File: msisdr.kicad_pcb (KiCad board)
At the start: 2 copper layers, 46.3 x 90.7 mm, 70 parts, among them J1 VCC_GPIO, J10 SMA_VHF1, J11 USB_OTG, J2 GPIO0, J3 GPIO1, J4 GPIO2, J5 GPIO3, J6 SMA_0_30MHZ, J7 SMA_30_60MHZ, J8 SMA_VHF2, J9 SMA_UHF, U1 msi2500, U2 msi001, U3 LP5900SDX-2.8, U4 AP7313-30SAG, Y1 24MHz

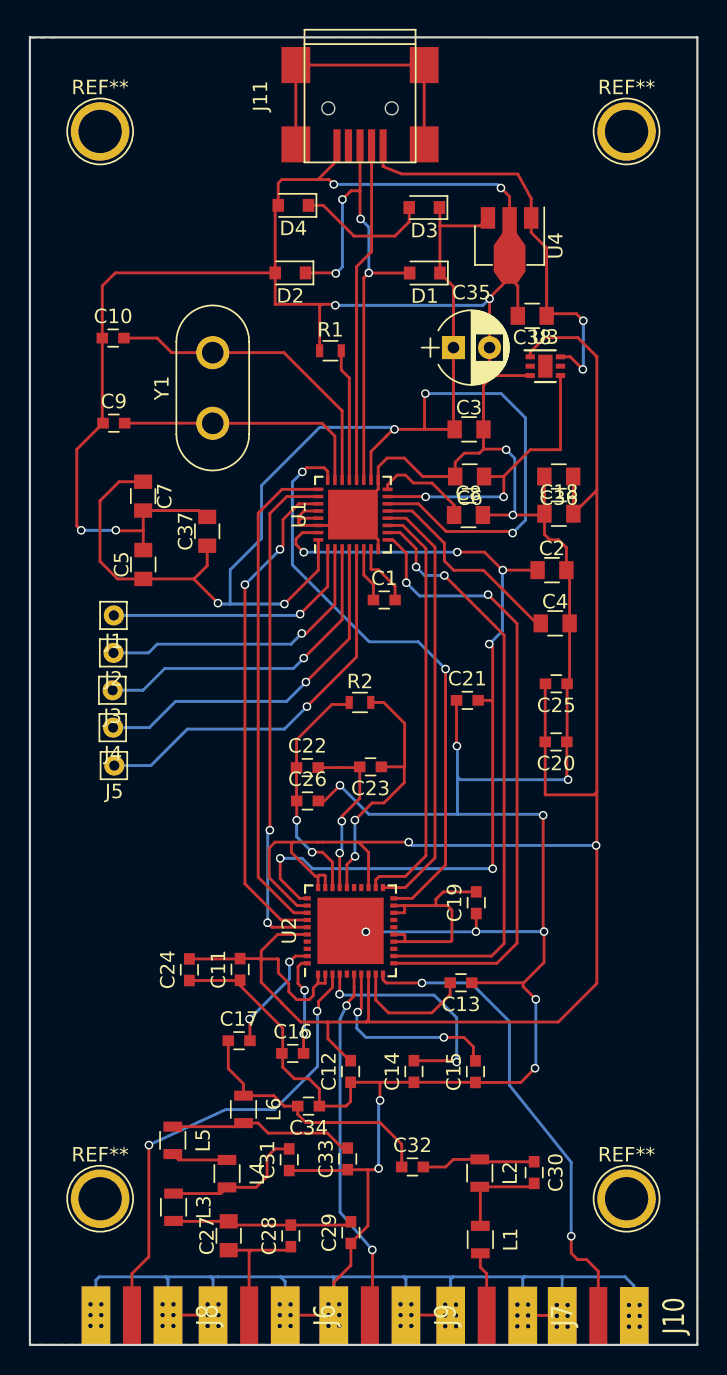
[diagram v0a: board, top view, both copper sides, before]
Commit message: use external oscillator repace xtal and add a led
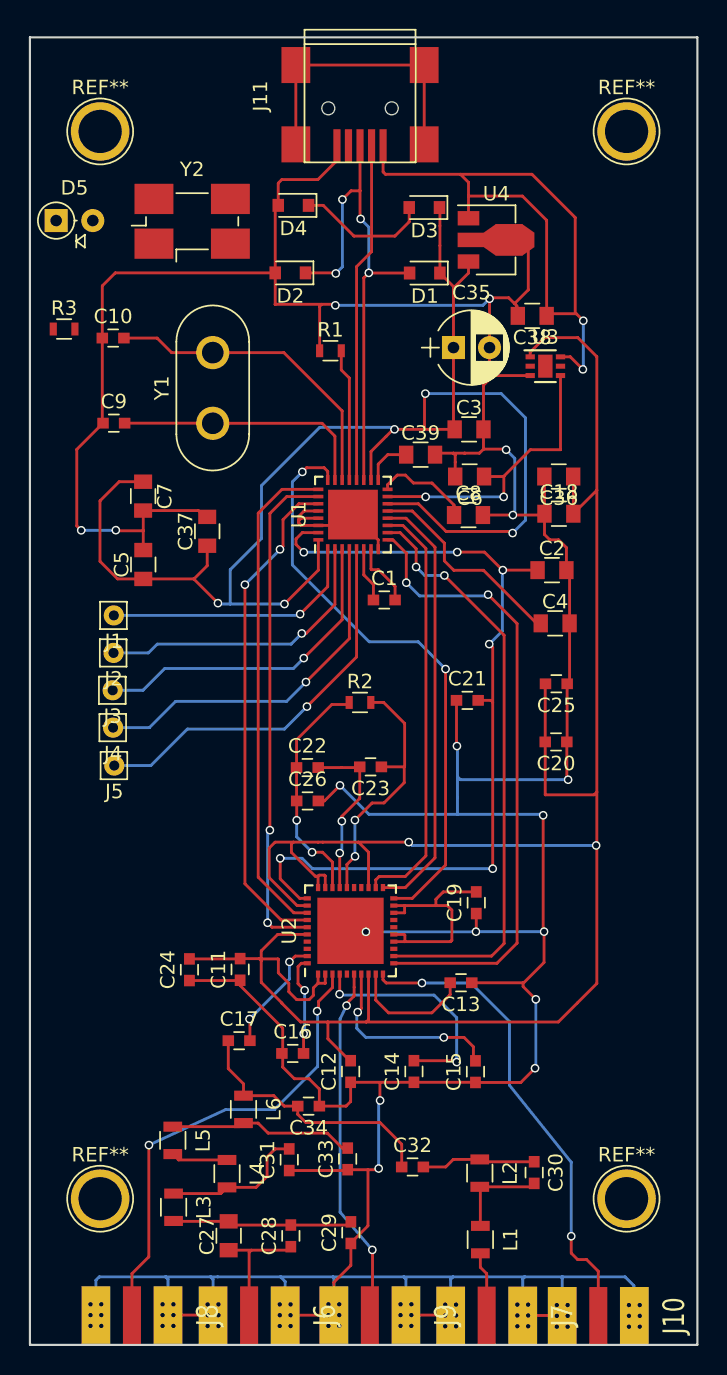
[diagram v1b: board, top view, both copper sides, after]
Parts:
- added C39: 1UF, Capacitors_SMD:C_0805, F.Cu at (140.2, 72.4)
- added D5: LED, Diodes_THT:D_DO-35_SOD27_P2.54mm_Vertical_AnodeUp, F.Cu at (115.0, 56.2)
- added R3: 512, Resistors_SMD:R_0603, F.Cu at (115.5, 63.7)
- added Y2: 24MHZ, Crystals:Crystal_SMD_0603-4pin_6.0x3.5mm_HandSoldering, F.Cu at (124.4, 56.2)
- moved U4 1.37 mm to (145.0, 57.5), turned to 0 degrees
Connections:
- U1 pad 17: GND -> Net-(C39-Pad1)
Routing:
- net GND: track 398.2 -> 374.7 mm, vias 19 -> 17
- net Net-(C38-Pad1): track 29.5 -> 47.1 mm
- net Net-(C39-Pad1): track 0.00 -> 3.31 mm
- net VDIG: track 105.7 -> 104.4 mm
- removed copper zone on B.Cu, net GND
- removed copper zone on F.Cu, net GND

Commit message: replace ldo and finish osc pcb layout
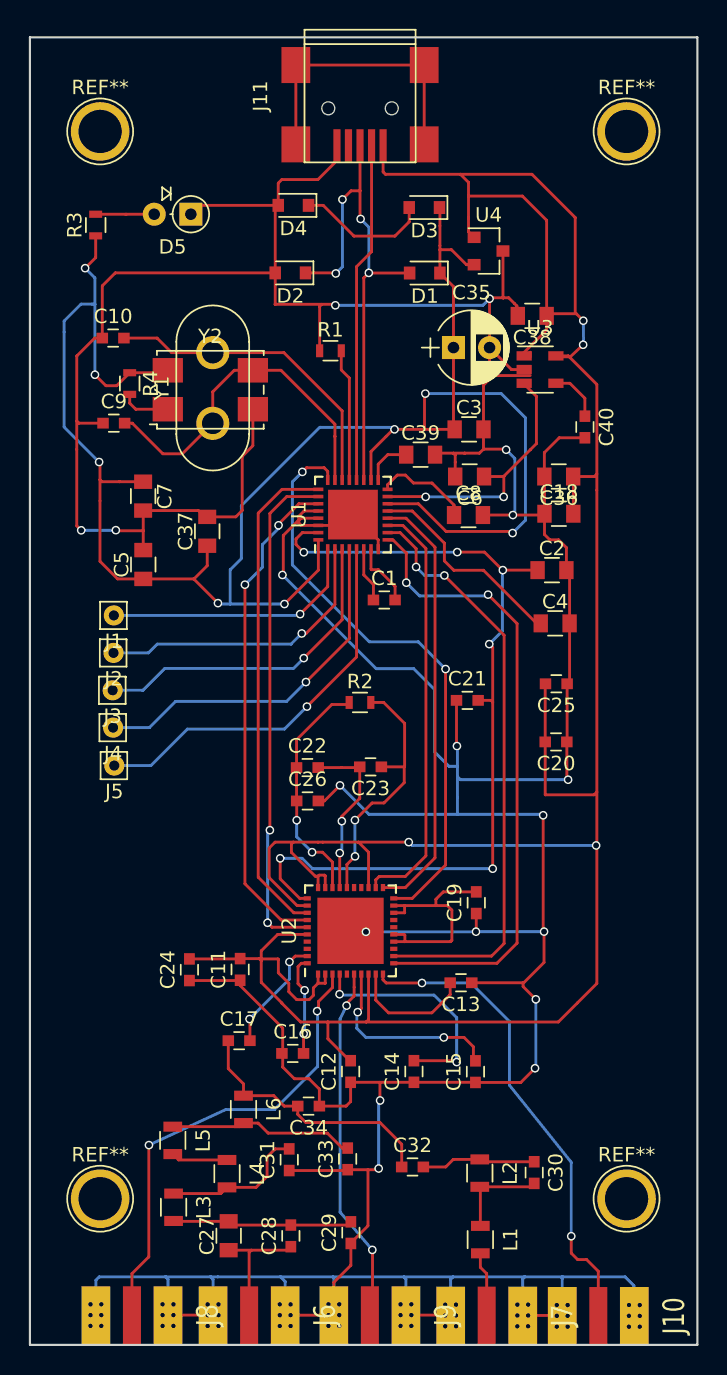
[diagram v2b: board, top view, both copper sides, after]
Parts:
- added C40: 22nF, Capacitors_SMD:C_0603, F.Cu at (151.6, 70.5)
- added R4: 10K, Resistors_SMD:R_0603, F.Cu at (120.0, 67.5)
- U3: value LP5900SDX-2.8 -> RT9193-28; footprint Housings_DFN_QFN:DFN-6-1EP_2x2mm_Pitch0.65mm -> TO_SOT_Packages_SMD:SOT-23-5
- U4: value AP7313-30SAG -> XC6206P302MR; footprint TO_SOT_Packages_SMD:SOT-89-3 -> TO_SOT_Packages_SMD:SOT-23
- Y2: footprint Crystals:Crystal_SMD_0603-4pin_6.0x3.5mm_HandSoldering -> Crystals:Crystal_SMD_7050-4pin_7.0x5.0mm
- moved Y2 11.7 mm to (125.6, 67.9)
- moved D5 9.35 mm to (124.3, 55.7), turned to 180 degrees
- moved R3 7.54 mm to (117.7, 56.5), turned to 90 degrees
- moved U4 0.78 mm to (144.9, 58.3)
- moved U3 0.44 mm to (148.5, 66.5)
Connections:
- U3 pad 1: VRF -> Net-(C38-Pad1)
- U3 pad 2: Net-(U3-Pad2) -> GND
- U3 pad 3: GND -> V18-SYNTH
- U3 pad 4: V18-SYNTH -> Net-(C40-Pad1)
- U3 pad 5: Net-(U3-Pad5) -> VRF
- U4 pad 2: GND -> VDIG
- U4 pad 3: VDIG -> GND
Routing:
- net GND: track 374.7 -> 423.9 mm, vias 17 -> 18
- net VDIG: track 104.4 -> 136.6 mm, vias 5 -> 8
- net Net-(C9-Pad2): track 18.0 -> 24.6 mm
- net Net-(D5-Pad2): track 0.00 -> 4.06 mm
- net Net-(C40-Pad1): track 0.00 -> 3.68 mm
- net Net-(R4-Pad2): track 0.00 -> 3.42 mm
- net V18-SYNTH: track 20.7 -> 18.8 mm
- net Net-(C38-Pad1): track 47.1 -> 46.4 mm, vias 2 -> 0
- net VRF: track 154.8 -> 154.3 mm, vias 2 -> 4

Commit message: finish drc
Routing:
- net VRF: track 154.3 -> 150.1 mm, vias 4 -> 2
- net GND: track 423.9 -> 420.5 mm
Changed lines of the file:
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@@
     (thickness 1.6)
     (drawings 5)
-    (tracks 912)
+    (tracks 905)
     (zones 0)
     (modules 76)
@@
   (segment (start 141.869 78.546) (end 139.639 76.316) (width 0.2) (layer F.Cu) (net 5))
   (segment (start 139.639 76.316) (end 137.929 76.316) (width 0.2) (layer F.Cu) (net 5))
-  (segment (start 147.4 67.46) (end 147.4 67.52) (width 0.2) (layer F.Cu) (net 6) (status C00000))
-  (segment (start 147.4 67.52) (end 148.25 68.37) (width 0.2) (layer F.Cu) (net 6) (status 400000))
+  (segment (start 147.4 67.46) (end 147.4 67.52) (width 0.2) (layer F.Cu) (net 6))
+  (segment (start 147.4 67.52) (end 148.25 68.37) (width 0.2) (layer F.Cu) (net 6))
   (segment (start 145.989 73.906) (end 147.829 72.066) (width 0.2) (layer F.Cu) (net 6))
   (segment (start 145.989 73.926) (end 145.989 73.906) (width 0.2) (layer F.Cu) (net 6))
@@
   (segment (start 134.279 71.15) (end 134.279 71.126) (width 0.2) (layer F.Cu) (net 7))
   (segment (start 125.799 70.226) (end 125.809 70.236) (width 0.2) (layer F.Cu) (net 7))
-  (segment (start 150.799 73.926) (end 152.264 73.926) (width 0.2) (layer F.Cu) (net 8) (status 400000))
+  (segment (start 150.799 73.926) (end 152.264 73.926) (width 0.2) (layer F.Cu) (net 8))
   (segment (start 152.264 73.926) (end 152.439 73.751) (width 0.2) (layer F.Cu) (net 8))
-  (segment (start 149.6 65.56) (end 150.46 65.56) (width 0.2) (layer F.Cu) (net 8) (status 400000))
+  (segment (start 149.6 65.56) (end 150.46 65.56) (width 0.2) (layer F.Cu) (net 8))
   (segment (start 150.46 65.56) (end 152.439 67.539) (width 0.2) (layer F.Cu) (net 8))
   (segment (start 152.439 67.539) (end 152.439 73.751) (width 0.2) (layer F.Cu) (net 8))
@@
   (segment (start 130.309 105.676) (end 129.169 106.816) (width 0.2) (layer F.Cu) (net 8))
   (segment (start 148.859 95.99676) (end 148.859 92.326) (width 0.2) (layer F.Cu) (net 8))
-  (segment (start 149.919 65.626) (end 150.59916 65.626) (width 0.2) (layer F.Cu) (net 8))
-  (segment (start 150.59916 65.626) (end 151.49 64.79) (width 0.2) (layer F.Cu) (net 8))
-  (via (at 151.49 64.79) (size 0.6) (drill 0.4) (layers F.Cu B.Cu) (net 8))
-  (segment (start 151.52048 64.75952) (end 151.50084 63.12408) (width 0.2) (layer B.Cu) (net 8))
-  (segment (start 151.49 64.79) (end 151.52048 64.75952) (width 0.2) (layer B.Cu) (net 8))
-  (via (at 151.50084 63.12408) (size 0.6) (drill 0.4) (layers F.Cu B.Cu) (net 8))
-  (segment (start 151.50084 63.12408) (end 151.01316 62.6364) (width 0.2) (layer F.Cu) (net 8))
   (segment (start 137.109 108.426) (end 137.109 110.22564) (width 0.2) (layer F.Cu) (net 9))
   (segment (start 142.269 109.84632) (end 142.269 109.026) (width 0.2) (layer F.Cu) (net 9))
@@
   (segment (start 123.09094 123.64208) (end 126.36762 123.64208) (width 0.2) (layer F.Cu) (net 33))
   (segment (start 126.36762 123.64208) (end 126.7968 123.2129) (width 0.2) (layer F.Cu) (net 33))
+  (segment (start 147.4 66.51) (end 145.038 66.51) (width 0.2) (layer F.Cu) (net 34) (status 400000))
+  (segment (start 145.038 66.51) (end 144.999 66.471) (width 0.2) (layer F.Cu) (net 34))
   (segment (start 131.7825 76.9725) (end 131.7375 76.9725) (width 0.2) (layer F.Cu) (net 34))
   (segment (start 142.19 94.02) (end 142.7734 94.02) (width 0.2) (layer B.Cu) (net 34))
@@
   (segment (start 130.7 78.01) (end 130.7 80.69) (width 0.2) (layer F.Cu) (net 34))
   (segment (start 131.7375 76.9725) (end 130.7 78.01) (width 0.2) (layer F.Cu) (net 34))
-  (segment (start 147.4 66.51) (end 146.523 66.51) (width 0.2) (layer F.Cu) (net 34) (status 400000))
-  (segment (start 146.523 66.51) (end 144.999 64.986) (width 0.2) (layer F.Cu) (net 34) (status 800000))
-  (segment (start 151.61 71.24) (end 149.83 71.24) (width 0.2) (layer F.Cu) (net 34) (status 400000))
-  (segment (start 148.799 72.271) (end 148.799 73.926) (width 0.2) (layer F.Cu) (net 34) (status 800000))
+  (segment (start 151.61 71.24) (end 149.83 71.24) (width 0.2) (layer F.Cu) (net 34))
+  (segment (start 148.799 72.271) (end 148.799 73.926) (width 0.2) (layer F.Cu) (net 34))
   (segment (start 149.83 71.24) (end 148.799 72.271) (width 0.2) (layer F.Cu) (net 34))
   (segment (start 145.93 58.29) (end 145.93 61.533) (width 0.2) (layer F.Cu) (net 34))
@@
   (segment (start 143.249 72.306) (end 143.29 72.306) (width 0.2) (layer F.Cu) (net 34))
   (segment (start 143.29 72.306) (end 144.299 72.306) (width 0.2) (layer F.Cu) (net 34))
-  (segment (start 147.819 66.926) (end 145.009 66.926) (width 0.2) (layer F.Cu) (net 34))
   (segment (start 145.009 66.926) (end 144.999 66.916) (width 0.2) (layer F.Cu) (net 34))
   (segment (start 144.579 70.656) (end 144.579 67.596) (width 0.2) (layer F.Cu) (net 34))
   (segment (start 144.579 67.596) (end 144.999 67.176) (width 0.2) (layer F.Cu) (net 34))
   (segment (start 144.999 67.176) (end 144.999 66.916) (width 0.2) (layer F.Cu) (net 34))
-  (segment (start 144.999 66.916) (end 144.999 64.986) (width 0.2) (layer F.Cu) (net 34))
+  (segment (start 144.999 66.916) (end 144.999 66.471) (width 0.2) (layer F.Cu) (net 34))
+  (segment (start 144.999 66.471) (end 144.999 64.986) (width 0.2) (layer F.Cu) (net 34))
   (segment (start 118.149 70.176) (end 118.199 70.226) (width 0.2) (layer F.Cu) (net 34))
   (segment (start 130.139 59.806) (end 119.049 59.806) (width 0.2) (layer F.Cu) (net 34))
@@
   (segment (start 119.81 55.74) (end 119.76 55.74) (width 0.2) (layer F.Cu) (net 61))
   (segment (start 119.81 55.74) (end 121.75 55.74) (width 0.2) (layer F.Cu) (net 61))
-  (segment (start 151.61 69.74) (end 151.61 68.5) (width 0.2) (layer F.Cu) (net 62) (status 400000))
-  (segment (start 150.57 67.46) (end 149.6 67.46) (width 0.2) (layer F.Cu) (net 62) (status 800000))
+  (segment (start 151.61 69.74) (end 151.61 68.5) (width 0.2) (layer F.Cu) (net 62))
+  (segment (start 150.57 67.46) (end 149.6 67.46) (width 0.2) (layer F.Cu) (net 62))
   (segment (start 151.61 68.5) (end 150.57 67.46) (width 0.2) (layer F.Cu) (net 62))
   (segment (start 122.69 69.26) (end 120.47 69.26) (width 0.2) (layer F.Cu) (net 63))
